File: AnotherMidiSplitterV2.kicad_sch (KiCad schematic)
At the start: 40 parts, among them J1 IN, J10 OUT, J11 OUT, J2 USB_power, J4 OUT, J5 OUT, J6 OUT, J7 OUT, J8 OUT, J9 OUT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

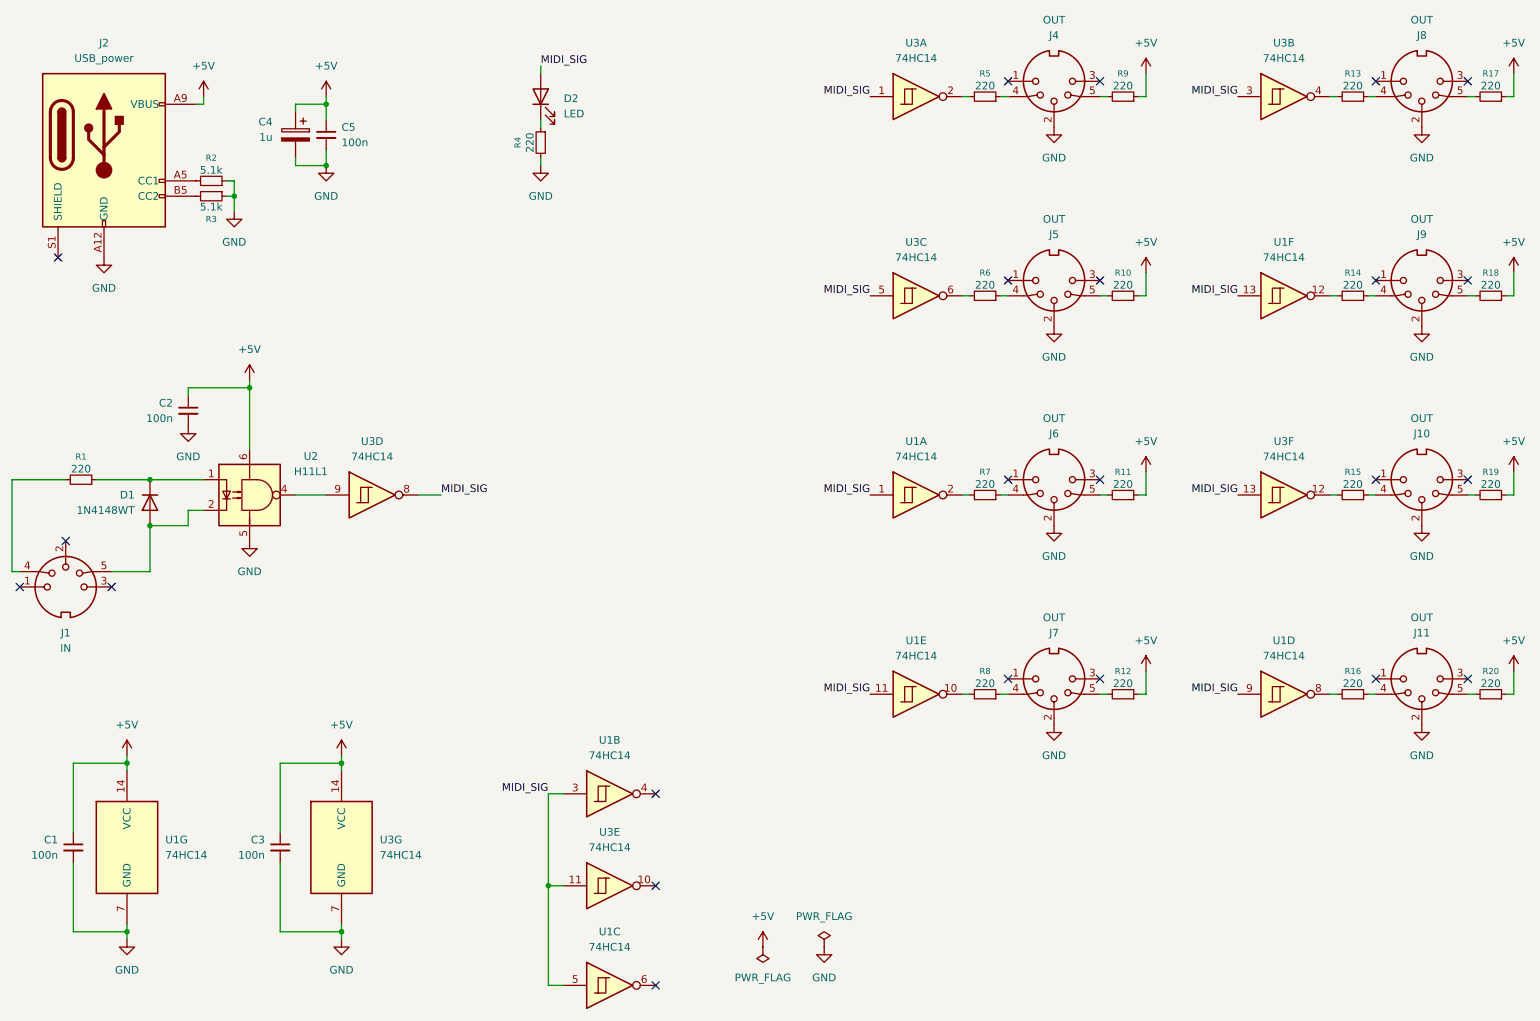
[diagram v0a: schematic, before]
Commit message: change elements to tht update layout
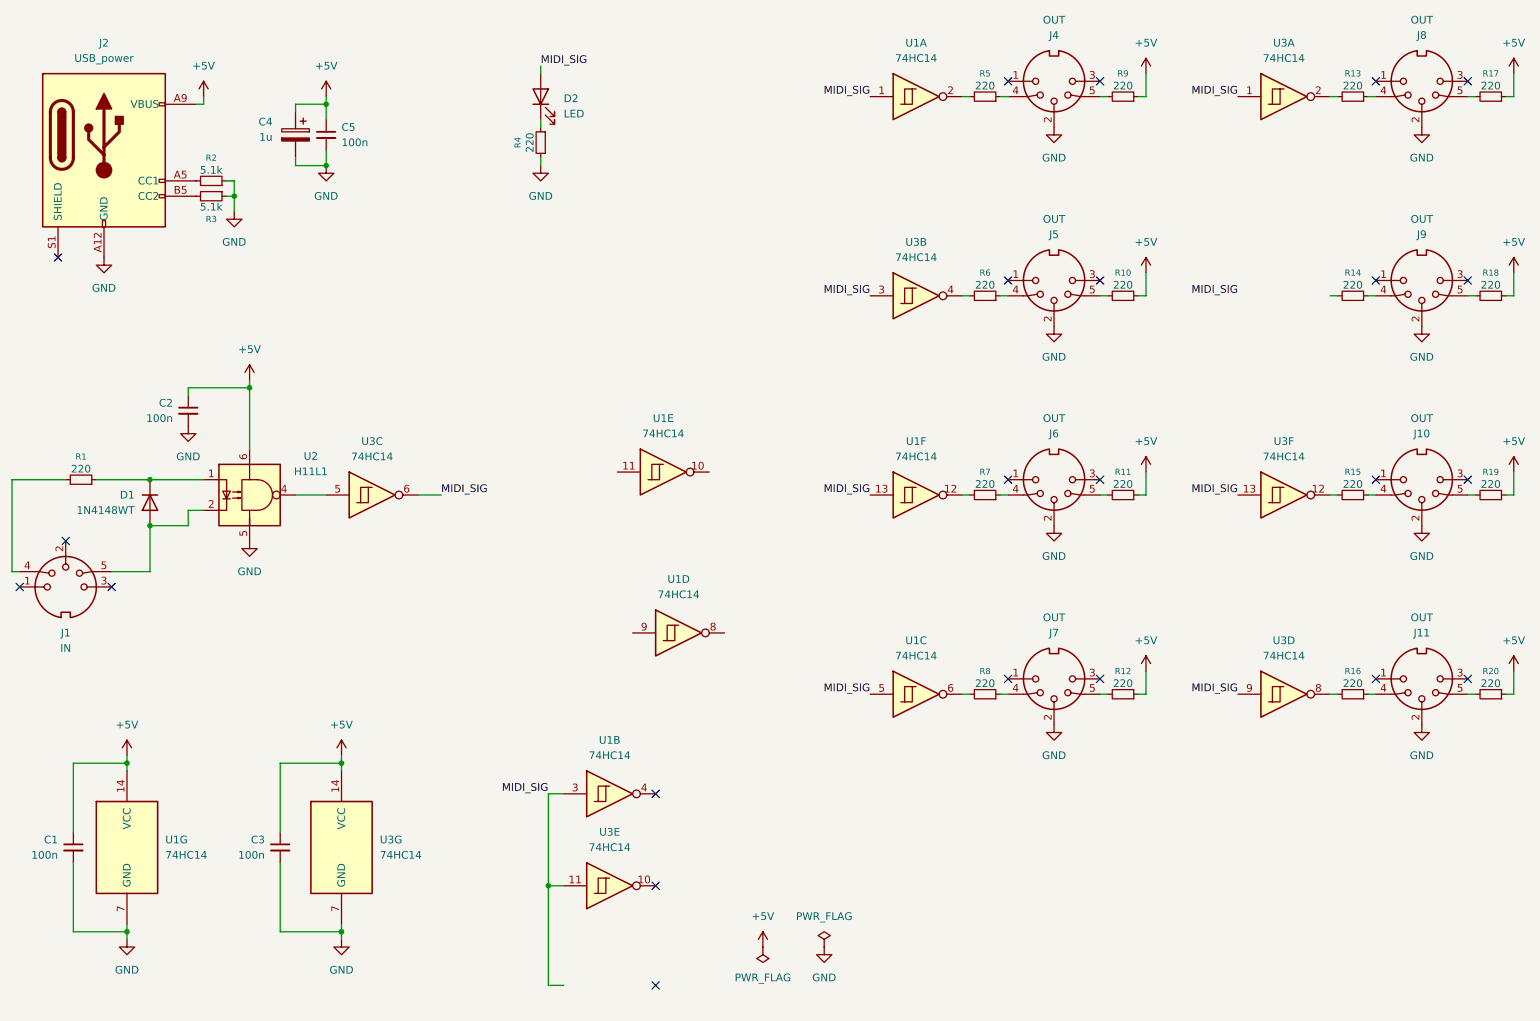
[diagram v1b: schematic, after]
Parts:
- C1, C2, C3, C5: footprint Capacitor_SMD:C_0805_2012Metric_Pad1.18x1.45mm_HandSolder -> Capacitor_THT:C_Disc_D3.0mm_W1.6mm_P2.50mm
- C4: footprint Capacitor_SMD:C_0805_2012Metric_Pad1.18x1.45mm_HandSolder -> Capacitor_THT:C_Radial_D4.0mm_H5.0mm_P1.50mm
- D1: footprint Diode_SMD:D_1206_3216Metric -> Diode_THT:D_A-405_P7.62mm_Horizontal
- D2: footprint LED_SMD:LED_1206_3216Metric -> LED_THT:LED_D3.0mm
- R1, R10, R11, R12, R13, R14, R15, R16, R17, R18, R19, R2, R20, R3, R4, R5, R6, R7, R8, R9: footprint Resistor_SMD:R_0603_1608Metric_Pad0.98x0.95mm_HandSolder -> Resistor_THT:R_Axial_DIN0207_L6.3mm_D2.5mm_P7.62mm_Horizontal
- U1, U3: footprint Package_SO:SO-14_5.3x10.2mm_P1.27mm -> Package_DIP:CERDIP-14_W7.62mm_SideBrazed_LongPads_Socket
- U2: footprint Package_DIP:DIP-6_W8.89mm_SMDSocket_LongPads -> Package_DIP:DIP-6_W7.62mm_Socket_LongPads
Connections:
- net MIDI_SIG: now also U3.6, U3.9; no longer U1.11, U1.9, U3.5, U3.8
- net at R14.2: no longer U1.12
- net at R16.2: now also U3.8; no longer U1.8
- net at U1.2: now also R5.2; no longer R7.2
- net at R13.2: now also U3.2; no longer U3.4
- net at U1.10: no longer R8.2
- net at R6.2: now also U3.4; no longer U3.6
- net at U2.4: now also U3.5; no longer U3.9
- net at U1.6: now also R8.2
- new net: R7.2, U1.12
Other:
- moved on the sheet: U1A, U1C, U1D, U1E, U1F, U3A, U3B, U3C, U3D
